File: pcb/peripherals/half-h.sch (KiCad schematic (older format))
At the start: 15 parts, among them Q201 RQ3E100BNTB, Q202 RQ3E100BNTB, U201 DGD0506A

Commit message: Layout finished and Gerbers generated
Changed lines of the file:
@@
 AR Path="/5B6E6A6C/5B7233C9" Ref="Q801"  Part="1"
 AR Path="/5B6E6A71/5B7233C9" Ref="Q901"  Part="1"
-F 0 "Q301" H 5788 3146 50  0000 L CNN
+F 0 "Q901" H 5788 3146 50  0000 L CNN
 F 1 "RQ3E100BNTB" H 5788 3055 50  0000 L CNN
 F 2 "peripherals:Rohm-HSMT8" H 5600 3200 50  0001 C CNN
@@
 AR Path="/5B6E6A6C/5B7233D1" Ref="U801"  Part="1"
 AR Path="/5B6E6A71/5B7233D1" Ref="U901"  Part="1"
-F 0 "U301" H 4250 3865 50  0000 C CNN
+F 0 "U901" H 4250 3865 50  0000 C CNN
 F 1 "DGD0506A" H 4250 3774 50  0000 C CNN
 F 2 "peripherals:Diodes-MSOP10" H 4250 3800 50  0001 C CNN
@@
 AR Path="/5B6E6A6C/5B7233E5" Ref="#PWR0807"  Part="1"
 AR Path="/5B6E6A71/5B7233E5" Ref="#PWR0907"  Part="1"
-F 0 "#PWR0307" H 5400 4000 50  0001 C CNN
+F 0 "#PWR0907" H 5400 4000 50  0001 C CNN
 F 1 "GND" H 5405 4077 50  0000 C CNN
 F 2 "" H 5400 4250 50  0001 C CNN
@@
 AR Path="/5B6E6A6C/5B7233F3" Ref="R801"  Part="1"
 AR Path="/5B6E6A71/5B7233F3" Ref="R901"  Part="1"
-F 0 "R301" V 4954 3100 50  0000 C CNN
+F 0 "R901" V 4954 3100 50  0000 C CNN
 F 1 "0" V 5045 3100 50  0000 C CNN
 F 2 "Resistors_SMD:R_0603_HandSoldering" H 5150 3100 50  0001 C CNN
@@
 AR Path="/5B6E6A6C/5B723403" Ref="#PWR0805"  Part="1"
 AR Path="/5B6E6A71/5B723403" Ref="#PWR0905"  Part="1"
-F 0 "#PWR0305" H 3700 3050 50  0001 C CNN
+F 0 "#PWR0905" H 3700 3050 50  0001 C CNN
 F 1 "GND" V 3705 3172 50  0000 R CNN
 F 2 "" H 3700 3300 50  0001 C CNN
@@
 AR Path="/5B6E6A6C/5B723409" Ref="R802"  Part="1"
 AR Path="/5B6E6A71/5B723409" Ref="R902"  Part="1"
-F 0 "R302" H 3541 3846 50  0000 R CNN
+F 0 "R902" H 3541 3846 50  0000 R CNN
 F 1 "10k" H 3541 3755 50  0000 R CNN
 F 2 "Resistors_SMD:R_0402" H 3600 3800 50  0001 C CNN
@@
 AR Path="/5B6E6A6C/5B723410" Ref="#PWR0806"  Part="1"
 AR Path="/5B6E6A71/5B723410" Ref="#PWR0906"  Part="1"
-F 0 "#PWR0306" H 3600 3750 50  0001 C CNN
+F 0 "#PWR0906" H 3600 3750 50  0001 C CNN
 F 1 "GND" H 3605 3827 50  0000 C CNN
 F 2 "" H 3600 4000 50  0001 C CNN
@@
 AR Path="/5B6E6A6C/5B723429" Ref="C805"  Part="1"
 AR Path="/5B6E6A71/5B723429" Ref="C905"  Part="1"
-F 0 "C305" V 4721 3300 50  0000 C CNN
+F 0 "C905" V 4721 3300 50  0000 C CNN
 F 1 "100nF" V 4812 3300 50  0000 C CNN
 F 2 "Capacitors_SMD:C_0402" H 4950 3300 50  0001 C CNN
@@
 AR Path="/5B6E6A6C/5B723443" Ref="C801"  Part="1"
 AR Path="/5B6E6A71/5B723443" Ref="C901"  Part="1"
-F 0 "C301" H 3992 2596 50  0000 L CNN
+F 0 "C901" H 3992 2596 50  0000 L CNN
 F 1 "10uF" H 3992 2505 50  0000 L CNN
 F 2 "Capacitors_SMD:CP_Elec_4x5.7" H 3900 2550 50  0001 C CNN
@@
 AR Path="/5B6E6A6C/5B72344C" Ref="#PWR0803"  Part="1"
 AR Path="/5B6E6A71/5B72344C" Ref="#PWR0903"  Part="1"
-F 0 "#PWR0303" H 4300 2450 50  0001 C CNN
+F 0 "#PWR0903" H 4300 2450 50  0001 C CNN
 F 1 "GND" H 4305 2527 50  0000 C CNN
 F 2 "" H 4300 2700 50  0001 C CNN
@@
 AR Path="/5B6E6A6C/5B723454" Ref="C803"  Part="1"
 AR Path="/5B6E6A71/5B723454" Ref="C903"  Part="1"
-F 0 "C303" H 5642 2596 50  0000 L CNN
+F 0 "C903" H 5642 2596 50  0000 L CNN
 F 1 "470uF" H 5642 2505 50  0000 L CNN
 F 2 "Capacitors_ThroughHole:CP_Radial_D10.0mm_P5.00mm" H 5550 2550 50  0001 C CNN
@@
 AR Path="/5B6E6A6C/5B72345C" Ref="C804"  Part="1"
 AR Path="/5B6E6A71/5B72345C" Ref="C904"  Part="1"
-F 0 "C304" H 6092 2596 50  0000 L CNN
+F 0 "C904" H 6092 2596 50  0000 L CNN
 F 1 "1000uF" H 6092 2505 50  0000 L CNN
 F 2 "Capacitors_ThroughHole:CP_Radial_D18.0mm_P7.50mm" H 6000 2550 50  0001 C CNN
@@
 AR Path="/5B6E6A6C/5B723466" Ref="#PWR0804"  Part="1"
 AR Path="/5B6E6A71/5B723466" Ref="#PWR0904"  Part="1"
-F 0 "#PWR0304" H 6000 2550 50  0001 C CNN
+F 0 "#PWR0904" H 6000 2550 50  0001 C CNN
 F 1 "GND" H 6005 2627 50  0000 C CNN
 F 2 "" H 6000 2800 50  0001 C CNN
@@
 AR Path="/5B6E6A6C/5B723472" Ref="L801"  Part="1"
 AR Path="/5B6E6A71/5B723472" Ref="L901"  Part="1"
-F 0 "L301" V 5285 2400 50  0000 C CNN
+F 0 "L901" V 5285 2400 50  0000 C CNN
 F 1 "100uH" V 5194 2400 50  0000 C CNN
 F 2 "Resistors_SMD:R_0805_HandSoldering" H 5100 2400 50  0001 C CNN
@@
 AR Path="/5B6E6A6C/5B72347E" Ref="#PWR0801"  Part="1"
 AR Path="/5B6E6A71/5B72347E" Ref="#PWR0901"  Part="1"
-F 0 "#PWR0301" H 5400 2150 50  0001 C CNN
+F 0 "#PWR0901" H 5400 2150 50  0001 C CNN
 F 1 "+BATT" H 5415 2473 50  0000 C CNN
 F 2 "" H 5400 2300 50  0001 C CNN
@@
 AR Path="/5B6E6A6C/5B723489" Ref="Q802"  Part="1"
 AR Path="/5B6E6A71/5B723489" Ref="Q902"  Part="1"
-F 0 "Q302" H 5788 3946 50  0000 L CNN
+F 0 "Q902" H 5788 3946 50  0000 L CNN
 F 1 "RQ3E100BNTB" H 5788 3855 50  0000 L CNN
 F 2 "peripherals:Rohm-HSMT8" H 5600 4000 50  0001 C CNN
@@
 AR Path="/5B6E6A6C/5B727333" Ref="R803"  Part="1"
 AR Path="/5B6E6A71/5B727333" Ref="R903"  Part="1"
-F 0 "R303" V 4054 3900 50  0000 C CNN
+F 0 "R903" V 4054 3900 50  0000 C CNN
 F 1 "0" V 4145 3900 50  0000 C CNN
 F 2 "Resistors_SMD:R_0603_HandSoldering" H 4250 3900 50  0001 C CNN
@@
 AR Path="/5B6E6A6C/5B728A25" Ref="#PWR0802"  Part="1"
 AR Path="/5B6E6A71/5B728A25" Ref="#PWR0902"  Part="1"
-F 0 "#PWR0302" H 3900 2450 50  0001 C CNN
+F 0 "#PWR0902" H 3900 2450 50  0001 C CNN
 F 1 "GND" H 3905 2527 50  0000 C CNN
 F 2 "" H 3900 2700 50  0001 C CNN
@@
 AR Path="/5B6E6A6C/5B72F72D" Ref="C802"  Part="1"
 AR Path="/5B6E6A71/5B72F72D" Ref="C902"  Part="1"
-F 0 "C302" H 4392 2596 50  0000 L CNN
+F 0 "C902" H 4392 2596 50  0000 L CNN
 F 1 "100nF" H 4392 2505 50  0000 L CNN
 F 2 "Capacitors_SMD:C_0402" H 4300 2550 50  0001 C CNN
@@
 AR Path="/5B6E6A6C/5B6EFABB" Ref="C806"  Part="1"
 AR Path="/5B6E6A71/5B6EFABB" Ref="C906"  Part="1"
-F 0 "C306" V 4721 3600 50  0000 C CNN
+F 0 "C906" V 4721 3600 50  0000 C CNN
 F 1 "DNP 0603" V 4812 3600 50  0000 C CNN
 F 2 "Capacitors_SMD:C_0603_HandSoldering" H 4950 3600 50  0001 C CNN
@@
 AR Path="/5B6E6A6C/5B6F8326" Ref="TP801"  Part="1"
 AR Path="/5B6E6A71/5B6F8326" Ref="TP901"  Part="1"
-F 0 "TP301" H 4692 3677 50  0000 R CNN
+F 0 "TP901" H 4692 3677 50  0000 R CNN
 F 1 "TestPoint_Alt" H 4692 3768 50  0000 R CNN
 F 2 "Measurement_Points:Measurement_Point_Round-SMD-Pad_Small" H 4950 3650 50  0001 C CNN
@@
 AR Path="/5B6E6A6C/5B6F99EB" Ref="TP802"  Part="1"
 AR Path="/5B6E6A71/5B6F99EB" Ref="TP902"  Part="1"
-F 0 "TP302" H 5242 3677 50  0000 R CNN
+F 0 "TP902" H 5242 3677 50  0000 R CNN
 F 1 "TestPoint_Alt" H 5242 3768 50  0000 R CNN
 F 2 "Measurement_Points:Measurement_Point_Round-SMD-Pad_Small" H 5500 3650 50  0001 C CNN
@@
 AR Path="/5B6E6A6C/5B6F59A4" Ref="#FLG0109"  Part="1"
 AR Path="/5B6E6A71/5B6F59A4" Ref="#FLG0110"  Part="1"
-F 0 "#FLG0104" H 4750 2375 50  0001 C CNN
+F 0 "#FLG0110" H 4750 2375 50  0001 C CNN
 F 1 "PWR_FLAG" H 4750 2474 50  0000 C CNN
 F 2 "" H 4750 2300 50  0001 C CNN
@@
 AR Path="/5B6E6A6C/5B6F73EE" Ref="#FLG0117"  Part="1"
 AR Path="/5B6E6A71/5B6F73EE" Ref="#FLG0118"  Part="1"
-F 0 "#FLG0112" H 5900 3525 50  0001 C CNN
+F 0 "#FLG0118" H 5900 3525 50  0001 C CNN
 F 1 "PWR_FLAG" H 5900 3624 50  0000 C CNN
 F 2 "" H 5900 3450 50  0001 C CNN

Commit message: Save before autotile
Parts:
- removed C203: 470uF, Capacitors_ThroughHole:CP_Radial_D10.0mm_P5.00mm, symbol Device:C_Small
- removed C204: 1000uF, Capacitors_ThroughHole:CP_Radial_D18.0mm_P7.50mm, symbol Device:C_Small
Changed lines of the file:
@@
 $Descr A4 11693 8268
 encoding utf-8
-Sheet 2 9
+Sheet 3 9
 Title ""
 Date ""
@@
 Wire Wire Line
 	4300 2650 4300 2700
-$Comp
-L Device:C_Small C?
-U 1 1 5B723454
-P 5550 2550
-AR Path="/5B723454" Ref="C?"  Part="1"
-AR Path="/5B7230C4/5B723454" Ref="C203"  Part="1"
-AR Path="/5B725BF5/5B723454" Ref="C?"  Part="1"
-AR Path="/5B6E69BA/5B723454" Ref="C303"  Part="1"
-AR Path="/5B6E69C9/5B723454" Ref="C403"  Part="1"
-AR Path="/5B6E69CE/5B723454" Ref="C503"  Part="1"
-AR Path="/5B6E6A62/5B723454" Ref="C603"  Part="1"
-AR Path="/5B6E6A67/5B723454" Ref="C703"  Part="1"
-AR Path="/5B6E6A6C/5B723454" Ref="C803"  Part="1"
-AR Path="/5B6E6A71/5B723454" Ref="C903"  Part="1"
-F 0 "C903" H 5642 2596 50  0000 L CNN
-F 1 "470uF" H 5642 2505 50  0000 L CNN
-F 2 "Capacitors_ThroughHole:CP_Radial_D10.0mm_P5.00mm" H 5550 2550 50  0001 C CNN
-F 3 "~" H 5550 2550 50  0001 C CNN
-F 4 "140-REA471M1EBK1012P" H 5550 2550 50  0001 C CNN "Mouser"
-	1    5550 2550
-	1    0    0    -1
-$EndComp
-$Comp
-L Device:C_Small C?
-U 1 1 5B72345C
-P 6000 2550
-AR Path="/5B72345C" Ref="C?"  Part="1"
-AR Path="/5B7230C4/5B72345C" Ref="C204"  Part="1"
-AR Path="/5B725BF5/5B72345C" Ref="C?"  Part="1"
-AR Path="/5B6E69BA/5B72345C" Ref="C304"  Part="1"
-AR Path="/5B6E69C9/5B72345C" Ref="C404"  Part="1"
-AR Path="/5B6E69CE/5B72345C" Ref="C504"  Part="1"
-AR Path="/5B6E6A62/5B72345C" Ref="C604"  Part="1"
-AR Path="/5B6E6A67/5B72345C" Ref="C704"  Part="1"
-AR Path="/5B6E6A6C/5B72345C" Ref="C804"  Part="1"
-AR Path="/5B6E6A71/5B72345C" Ref="C904"  Part="1"
-F 0 "C904" H 6092 2596 50  0000 L CNN
-F 1 "1000uF" H 6092 2505 50  0000 L CNN
-F 2 "Capacitors_ThroughHole:CP_Radial_D18.0mm_P7.50mm" H 6000 2550 50  0001 C CNN
-F 3 "~" H 6000 2550 50  0001 C CNN
-F 4 "598-108SAK025M" H 6000 2550 50  0001 C CNN "Mouser"
-	1    6000 2550
-	1    0    0    -1
-$EndComp
-Wire Wire Line
-	5550 2450 5550 2400
-Wire Wire Line
-	6000 2450 6000 2400
-Wire Wire Line
-	6000 2400 5550 2400
-$Comp
-L power:GND #PWR?
-U 1 1 5B723466
-P 6000 2800
-AR Path="/5B723466" Ref="#PWR?"  Part="1"
-AR Path="/5B7230C4/5B723466" Ref="#PWR0204"  Part="1"
-AR Path="/5B725BF5/5B723466" Ref="#PWR?"  Part="1"
-AR Path="/5B6E69BA/5B723466" Ref="#PWR0304"  Part="1"
-AR Path="/5B6E69C9/5B723466" Ref="#PWR0404"  Part="1"
-AR Path="/5B6E69CE/5B723466" Ref="#PWR0504"  Part="1"
-AR Path="/5B6E6A62/5B723466" Ref="#PWR0604"  Part="1"
-AR Path="/5B6E6A67/5B723466" Ref="#PWR0704"  Part="1"
-AR Path="/5B6E6A6C/5B723466" Ref="#PWR0804"  Part="1"
-AR Path="/5B6E6A71/5B723466" Ref="#PWR0904"  Part="1"
-F 0 "#PWR0904" H 6000 2550 50  0001 C CNN
-F 1 "GND" H 6005 2627 50  0000 C CNN
-F 2 "" H 6000 2800 50  0001 C CNN
-F 3 "" H 6000 2800 50  0001 C CNN
-	1    6000 2800
-	1    0    0    -1
-$EndComp
-Wire Wire Line
-	5550 2650 5550 2700
-Wire Wire Line
-	5550 2700 6000 2700
-Wire Wire Line
-	6000 2700 6000 2800
-Wire Wire Line
-	6000 2650 6000 2700
-Connection ~ 6000 2700
 Wire Wire Line
 	5400 2300 5400 2400
@@
 Wire Wire Line
 	3250 3500 3800 3500
-Wire Wire Line
-	5400 2400 5550 2400
-Connection ~ 5550 2400
 $Comp
 L peripherals:Q_NMOS_SSSGDDDD Q?

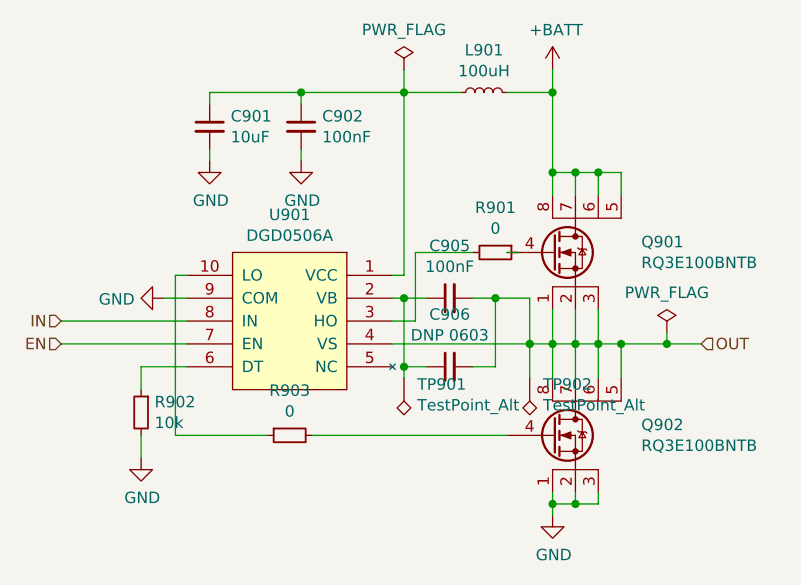
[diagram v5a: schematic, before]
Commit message: Redesign peripheral PCB, simulate photodiode circuit
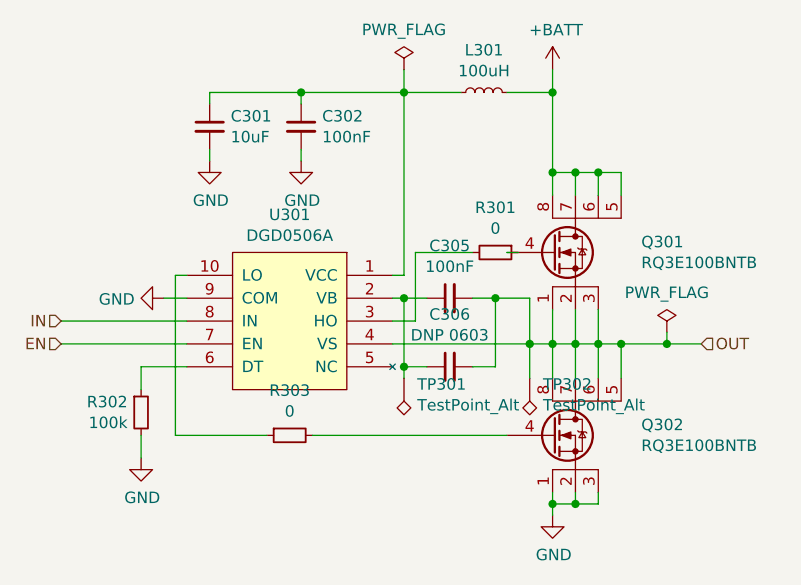
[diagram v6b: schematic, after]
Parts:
- R202: value 10k -> 100k; Mouser 603-RC0402JR-0710KL -> 603-RC0402JR-13100KL
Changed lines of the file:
@@
 AR Path="/5B6E6A6C/5B7233C9" Ref="Q801"  Part="1"
 AR Path="/5B6E6A71/5B7233C9" Ref="Q901"  Part="1"
-F 0 "Q901" H 5788 3146 50  0000 L CNN
+F 0 "Q301" H 5788 3146 50  0000 L CNN
 F 1 "RQ3E100BNTB" H 5788 3055 50  0000 L CNN
 F 2 "peripherals:Rohm-HSMT8" H 5600 3200 50  0001 C CNN
@@
 AR Path="/5B6E6A6C/5B7233D1" Ref="U801"  Part="1"
 AR Path="/5B6E6A71/5B7233D1" Ref="U901"  Part="1"
-F 0 "U901" H 4250 3865 50  0000 C CNN
+F 0 "U301" H 4250 3865 50  0000 C CNN
 F 1 "DGD0506A" H 4250 3774 50  0000 C CNN
 F 2 "peripherals:Diodes-MSOP10" H 4250 3800 50  0001 C CNN
@@
 AR Path="/5B6E6A6C/5B7233E5" Ref="#PWR0807"  Part="1"
 AR Path="/5B6E6A71/5B7233E5" Ref="#PWR0907"  Part="1"
-F 0 "#PWR0907" H 5400 4000 50  0001 C CNN
+F 0 "#PWR0307" H 5400 4000 50  0001 C CNN
 F 1 "GND" H 5405 4077 50  0000 C CNN
 F 2 "" H 5400 4250 50  0001 C CNN
@@
 AR Path="/5B6E6A6C/5B7233F3" Ref="R801"  Part="1"
 AR Path="/5B6E6A71/5B7233F3" Ref="R901"  Part="1"
-F 0 "R901" V 4954 3100 50  0000 C CNN
+F 0 "R301" V 4954 3100 50  0000 C CNN
 F 1 "0" V 5045 3100 50  0000 C CNN
 F 2 "Resistors_SMD:R_0603_HandSoldering" H 5150 3100 50  0001 C CNN
@@
 AR Path="/5B6E6A6C/5B723403" Ref="#PWR0805"  Part="1"
 AR Path="/5B6E6A71/5B723403" Ref="#PWR0905"  Part="1"
-F 0 "#PWR0905" H 3700 3050 50  0001 C CNN
+F 0 "#PWR0305" H 3700 3050 50  0001 C CNN
 F 1 "GND" V 3705 3172 50  0000 R CNN
 F 2 "" H 3700 3300 50  0001 C CNN
@@
 AR Path="/5B6E6A6C/5B723409" Ref="R802"  Part="1"
 AR Path="/5B6E6A71/5B723409" Ref="R902"  Part="1"
-F 0 "R902" H 3541 3846 50  0000 R CNN
-F 1 "10k" H 3541 3755 50  0000 R CNN
+F 0 "R302" H 3541 3846 50  0000 R CNN
+F 1 "100k" H 3541 3755 50  0000 R CNN
 F 2 "Resistors_SMD:R_0402" H 3600 3800 50  0001 C CNN
 F 3 "~" H 3600 3800 50  0001 C CNN
-F 4 "603-RC0402JR-0710KL" H 3600 3800 50  0001 C CNN "Mouser"
+F 4 "603-RC0402JR-13100KL" H 3600 3800 50  0001 C CNN "Mouser"
 	1    3600 3800
-	-1   0    0    -1
+	1    0    0    -1
 $EndComp
 $Comp
@@
 AR Path="/5B6E6A6C/5B723410" Ref="#PWR0806"  Part="1"
 AR Path="/5B6E6A71/5B723410" Ref="#PWR0906"  Part="1"
-F 0 "#PWR0906" H 3600 3750 50  0001 C CNN
+F 0 "#PWR0306" H 3600 3750 50  0001 C CNN
 F 1 "GND" H 3605 3827 50  0000 C CNN
 F 2 "" H 3600 4000 50  0001 C CNN
@@
 AR Path="/5B6E6A6C/5B723429" Ref="C805"  Part="1"
 AR Path="/5B6E6A71/5B723429" Ref="C905"  Part="1"
-F 0 "C905" V 4721 3300 50  0000 C CNN
+F 0 "C305" V 4721 3300 50  0000 C CNN
 F 1 "100nF" V 4812 3300 50  0000 C CNN
 F 2 "Capacitors_SMD:C_0402" H 4950 3300 50  0001 C CNN
@@
 AR Path="/5B6E6A6C/5B723443" Ref="C801"  Part="1"
 AR Path="/5B6E6A71/5B723443" Ref="C901"  Part="1"
-F 0 "C901" H 3992 2596 50  0000 L CNN
+F 0 "C301" H 3992 2596 50  0000 L CNN
 F 1 "10uF" H 3992 2505 50  0000 L CNN
 F 2 "Capacitors_SMD:CP_Elec_4x5.7" H 3900 2550 50  0001 C CNN
@@
 AR Path="/5B6E6A6C/5B72344C" Ref="#PWR0803"  Part="1"
 AR Path="/5B6E6A71/5B72344C" Ref="#PWR0903"  Part="1"
-F 0 "#PWR0903" H 4300 2450 50  0001 C CNN
+F 0 "#PWR0303" H 4300 2450 50  0001 C CNN
 F 1 "GND" H 4305 2527 50  0000 C CNN
 F 2 "" H 4300 2700 50  0001 C CNN
@@
 AR Path="/5B6E6A6C/5B723472" Ref="L801"  Part="1"
 AR Path="/5B6E6A71/5B723472" Ref="L901"  Part="1"
-F 0 "L901" V 5285 2400 50  0000 C CNN
+F 0 "L301" V 5285 2400 50  0000 C CNN
 F 1 "100uH" V 5194 2400 50  0000 C CNN
 F 2 "Resistors_SMD:R_0805_HandSoldering" H 5100 2400 50  0001 C CNN
@@
 AR Path="/5B6E6A6C/5B72347E" Ref="#PWR0801"  Part="1"
 AR Path="/5B6E6A71/5B72347E" Ref="#PWR0901"  Part="1"
-F 0 "#PWR0901" H 5400 2150 50  0001 C CNN
+F 0 "#PWR0301" H 5400 2150 50  0001 C CNN
 F 1 "+BATT" H 5415 2473 50  0000 C CNN
 F 2 "" H 5400 2300 50  0001 C CNN
@@
 AR Path="/5B6E6A6C/5B723489" Ref="Q802"  Part="1"
 AR Path="/5B6E6A71/5B723489" Ref="Q902"  Part="1"
-F 0 "Q902" H 5788 3946 50  0000 L CNN
+F 0 "Q302" H 5788 3946 50  0000 L CNN
 F 1 "RQ3E100BNTB" H 5788 3855 50  0000 L CNN
 F 2 "peripherals:Rohm-HSMT8" H 5600 4000 50  0001 C CNN
@@
 AR Path="/5B6E6A6C/5B727333" Ref="R803"  Part="1"
 AR Path="/5B6E6A71/5B727333" Ref="R903"  Part="1"
-F 0 "R903" V 4054 3900 50  0000 C CNN
+F 0 "R303" V 4054 3900 50  0000 C CNN
 F 1 "0" V 4145 3900 50  0000 C CNN
 F 2 "Resistors_SMD:R_0603_HandSoldering" H 4250 3900 50  0001 C CNN
@@
 AR Path="/5B6E6A6C/5B728A25" Ref="#PWR0802"  Part="1"
 AR Path="/5B6E6A71/5B728A25" Ref="#PWR0902"  Part="1"
-F 0 "#PWR0902" H 3900 2450 50  0001 C CNN
+F 0 "#PWR0302" H 3900 2450 50  0001 C CNN
 F 1 "GND" H 3905 2527 50  0000 C CNN
 F 2 "" H 3900 2700 50  0001 C CNN
@@
 AR Path="/5B6E6A6C/5B72F72D" Ref="C802"  Part="1"
 AR Path="/5B6E6A71/5B72F72D" Ref="C902"  Part="1"
-F 0 "C902" H 4392 2596 50  0000 L CNN
+F 0 "C302" H 4392 2596 50  0000 L CNN
 F 1 "100nF" H 4392 2505 50  0000 L CNN
 F 2 "Capacitors_SMD:C_0402" H 4300 2550 50  0001 C CNN
@@
 AR Path="/5B6E6A6C/5B6EFABB" Ref="C806"  Part="1"
 AR Path="/5B6E6A71/5B6EFABB" Ref="C906"  Part="1"
-F 0 "C906" V 4721 3600 50  0000 C CNN
+F 0 "C306" V 4721 3600 50  0000 C CNN
 F 1 "DNP 0603" V 4812 3600 50  0000 C CNN
 F 2 "Capacitors_SMD:C_0603_HandSoldering" H 4950 3600 50  0001 C CNN
@@
 AR Path="/5B6E6A6C/5B6F8326" Ref="TP801"  Part="1"
 AR Path="/5B6E6A71/5B6F8326" Ref="TP901"  Part="1"
-F 0 "TP901" H 4692 3677 50  0000 R CNN
+F 0 "TP301" H 4692 3677 50  0000 R CNN
 F 1 "TestPoint_Alt" H 4692 3768 50  0000 R CNN
 F 2 "Measurement_Points:Measurement_Point_Round-SMD-Pad_Small" H 4950 3650 50  0001 C CNN
@@
 AR Path="/5B6E6A6C/5B6F99EB" Ref="TP802"  Part="1"
 AR Path="/5B6E6A71/5B6F99EB" Ref="TP902"  Part="1"
-F 0 "TP902" H 5242 3677 50  0000 R CNN
+F 0 "TP302" H 5242 3677 50  0000 R CNN
 F 1 "TestPoint_Alt" H 5242 3768 50  0000 R CNN
 F 2 "Measurement_Points:Measurement_Point_Round-SMD-Pad_Small" H 5500 3650 50  0001 C CNN
@@
 AR Path="/5B6E6A6C/5B6F59A4" Ref="#FLG0109"  Part="1"
 AR Path="/5B6E6A71/5B6F59A4" Ref="#FLG0110"  Part="1"
-F 0 "#FLG0110" H 4750 2375 50  0001 C CNN
+F 0 "#FLG0104" H 4750 2375 50  0001 C CNN
 F 1 "PWR_FLAG" H 4750 2474 50  0000 C CNN
 F 2 "" H 4750 2300 50  0001 C CNN
@@
 AR Path="/5B6E6A6C/5B6F73EE" Ref="#FLG0117"  Part="1"
 AR Path="/5B6E6A71/5B6F73EE" Ref="#FLG0118"  Part="1"
-F 0 "#FLG0118" H 5900 3525 50  0001 C CNN
+F 0 "#FLG0112" H 5900 3525 50  0001 C CNN
 F 1 "PWR_FLAG" H 5900 3624 50  0000 C CNN
 F 2 "" H 5900 3450 50  0001 C CNN
